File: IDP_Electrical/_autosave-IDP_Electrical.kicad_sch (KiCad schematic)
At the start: 28 parts, among them M1 DC Motor Symbol, M2 DC Motor Symbol, U1 SER0038, U2 SER0038

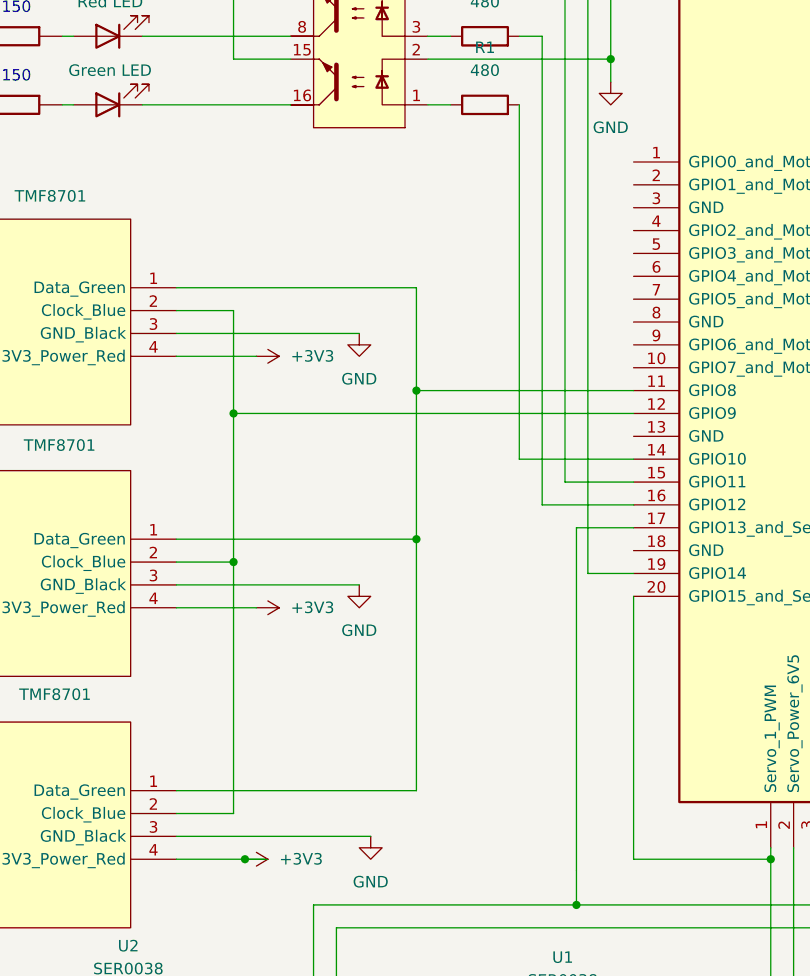
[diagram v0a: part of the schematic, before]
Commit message: updated schematic wiring
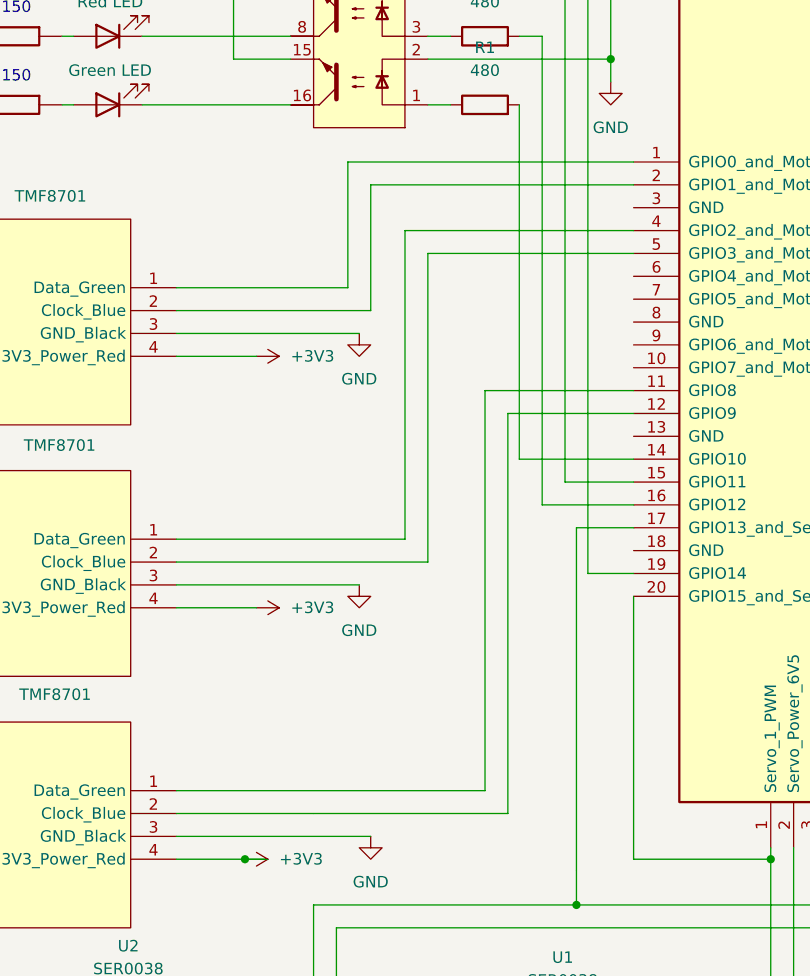
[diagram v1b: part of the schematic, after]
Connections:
- net at A1.11 (GPIO8), Sensor6.1 (Data_Green): no longer Sensor5.1 (Data_Green), Sensor7.1 (Data_Green)
- net at A1.12 (GPIO9), Sensor6.2 (Clock_Blue): no longer Sensor5.2 (Clock_Blue), Sensor7.2 (Clock_Blue)
- net at A1.4 (GPIO2_and_Motor_2_PWM): now also Sensor5.1 (Data_Green)
- net at A1.5 (GPIO3_and_Motor_2_Direction): now also Sensor5.2 (Clock_Blue)
- new net: A1.1 (Motor_1_6V5), Sensor7.1 (Data_Green)
- new net: A1.2 (Motor_4_12V), Sensor7.2 (Clock_Blue)
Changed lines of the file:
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@@
-	)
-	(junction
-		(at 68.58 97.79)
-		(diameter 0)
-		(color 0 0 0 0)
-	)
-	(junction
-		(at 68.58 114.3)
-		(diameter 0)
-		(color 0 0 0 0)
 	)
 	(junction
@@
 	)
 	(junction
-		(at 48.26 116.84)
-		(diameter 0)
-		(color 0 0 0 0)
-	)
-	(junction
 		(at 90.17 53.34)
 		(diameter 0)
@@
 		(color 0 0 0 0)
 	)
-	(junction
-		(at 48.26 100.33)
-		(diameter 0)
-		(color 0 0 0 0)
-	)
 	(wire
 		(pts
@@
 	(wire
 		(pts
-			(xy 41.91 144.78) (xy 48.26 144.78)
+			(xy 41.91 144.78) (xy 78.74 144.78)
 		)
 		(stroke
@@
 	(wire
 		(pts
-			(xy 68.58 114.3) (xy 68.58 97.79)
-		)
-		(stroke
-			(width 0)
-			(type default)
-		)
-	)
-	(wire
-		(pts
 			(xy 151.13 148.59) (xy 151.13 180.34)
 		)
@@
 	(wire
 		(pts
+			(xy 76.2 97.79) (xy 92.71 97.79)
+		)
+		(stroke
+			(width 0)
+			(type default)
+		)
+	)
+	(wire
+		(pts
 			(xy 85.09 107.95) (xy 92.71 107.95)
 		)
@@
 	(wire
 		(pts
-			(xy 48.26 116.84) (xy 48.26 144.78)
-		)
-		(stroke
-			(width 0)
-			(type default)
-		)
-	)
-	(wire
-		(pts
 			(xy 82.55 110.49) (xy 92.71 110.49)
 		)
@@
 	(wire
 		(pts
+			(xy 78.74 100.33) (xy 92.71 100.33)
+		)
+		(stroke
+			(width 0)
+			(type default)
+		)
+	)
+	(wire
+		(pts
 			(xy 110.49 185.42) (xy 110.49 148.59)
 		)
@@
 	(wire
 		(pts
-			(xy 41.91 116.84) (xy 48.26 116.84)
-		)
-		(stroke
-			(width 0)
-			(type default)
-		)
-	)
-	(wire
-		(pts
-			(xy 41.91 114.3) (xy 68.58 114.3)
+			(xy 41.91 116.84) (xy 69.85 116.84)
+		)
+		(stroke
+			(width 0)
+			(type default)
+		)
+	)
+	(wire
+		(pts
+			(xy 41.91 114.3) (xy 67.31 114.3)
 		)
 		(stroke
@@
 	(wire
 		(pts
+			(xy 41.91 86.36) (xy 60.96 86.36)
+		)
+		(stroke
+			(width 0)
+			(type default)
+		)
+	)
+	(wire
+		(pts
 			(xy 168.91 118.11) (xy 204.47 118.11)
 		)
@@
 	(wire
 		(pts
-			(xy 41.91 88.9) (xy 48.26 88.9)
+			(xy 41.91 88.9) (xy 63.5 88.9)
 		)
 		(stroke
@@
 	(wire
 		(pts
-			(xy 92.71 100.33) (xy 48.26 100.33)
-		)
-		(stroke
-			(width 0)
-			(type default)
-		)
-	)
-	(wire
-		(pts
 			(xy 29.21 50.8) (xy 30.48 50.8)
 		)
@@
 	(wire
 		(pts
+			(xy 92.71 74.93) (xy 63.5 74.93)
+		)
+		(stroke
+			(width 0)
+			(type default)
+		)
+	)
+	(wire
+		(pts
 			(xy 153.67 148.59) (xy 153.67 161.29)
 		)
@@
 	(wire
 		(pts
+			(xy 63.5 74.93) (xy 63.5 88.9)
+		)
+		(stroke
+			(width 0)
+			(type default)
+		)
+	)
+	(wire
+		(pts
 			(xy 214.63 113.03) (xy 209.55 113.03)
 		)
@@
 	(wire
 		(pts
-			(xy 68.58 97.79) (xy 92.71 97.79)
-		)
-		(stroke
-			(width 0)
-			(type default)
-		)
-	)
-	(wire
-		(pts
 			(xy 53.34 186.69) (xy 57.15 186.69)
 		)
@@
 	(wire
 		(pts
-			(xy 68.58 114.3) (xy 68.58 142.24)
-		)
-		(stroke
-			(width 0)
-			(type default)
-		)
-	)
-	(wire
-		(pts
 			(xy 72.39 58.42) (xy 69.85 58.42)
 		)
@@
 	(wire
 		(pts
-			(xy 68.58 86.36) (xy 68.58 97.79)
+			(xy 76.2 142.24) (xy 76.2 97.79)
 		)
 		(stroke
@@
 	(wire
 		(pts
-			(xy 48.26 100.33) (xy 48.26 88.9)
-		)
-		(stroke
-			(width 0)
-			(type default)
-		)
-	)
-	(wire
-		(pts
 			(xy 48.26 53.34) (xy 54.61 53.34)
 		)
@@
 	(wire
 		(pts
+			(xy 67.31 80.01) (xy 67.31 114.3)
+		)
+		(stroke
+			(width 0)
+			(type default)
+		)
+	)
+	(wire
+		(pts
 			(xy 189.23 105.41) (xy 189.23 130.81)
 		)
@@
 	(wire
 		(pts
-			(xy 41.91 86.36) (xy 68.58 86.36)
+			(xy 92.71 82.55) (xy 69.85 82.55)
 		)
 		(stroke
@@
 	(wire
 		(pts
-			(xy 41.91 142.24) (xy 68.58 142.24)
+			(xy 60.96 86.36) (xy 60.96 72.39)
+		)
+		(stroke
+			(width 0)
+			(type default)
+		)
+	)
+	(wire
+		(pts
+			(xy 41.91 142.24) (xy 76.2 142.24)
 		)
 		(stroke
@@
 	(wire
 		(pts
+			(xy 78.74 144.78) (xy 78.74 100.33)
+		)
+		(stroke
+			(width 0)
+			(type default)
+		)
+	)
+	(wire
+		(pts
 			(xy 48.26 45.72) (xy 54.61 45.72)
 		)
@@
 	(wire
 		(pts
+			(xy 69.85 82.55) (xy 69.85 116.84)
+		)
+		(stroke
+			(width 0)
+			(type default)
+		)
+	)
+	(wire
+		(pts
 			(xy 19.05 43.18) (xy 30.48 43.18)
 		)
@@
 	(wire
 		(pts
-			(xy 48.26 100.33) (xy 48.26 116.84)
-		)
-		(stroke
-			(width 0)
-			(type default)
-		)
-	)
-	(wire
-		(pts
 			(xy 172.72 100.33) (xy 168.91 100.33)
 		)
@@
 	(wire
 		(pts
+			(xy 60.96 72.39) (xy 92.71 72.39)
+		)
+		(stroke
+			(width 0)
+			(type default)
+		)
+	)
+	(wire
+		(pts
 			(xy 86.36 154.94) (xy 86.36 151.13)
 		)
@@
 		)
 		(stroke
+			(width 0)
+			(type default)
+		)
+	)
+	(wire
+		(pts
+			(xy 67.31 80.01) (xy 92.71 80.01)
+		)
+		(stroke
